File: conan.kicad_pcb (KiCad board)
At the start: 4 copper layers, 313 parts, among them J1 JST-XH, J10 PWM11, J11 PWM3, J12 PWM7, J13 PWM12, J14 PWM4, J15 PWM8, J16 Stepper, J17 Stepper, J18 Stepper, J19 Stepper, J2 JST-XH, J20 Stepper, J21 Stepper, J22 Boot, J23 UART1, J24 UART2, J25 USB_B_Micro, J26 Endstop 1, J27 Endstop 2, J28 Endstop 3, J29 Endstop 4, J3 JTAG, J30 Endstop 5, J31 Endstop 6, J32 Endstop 7, J33 Endstop 8, J34 Watchdog, J35 Thermistor 1, J36 Thermistor 2, J37 Thermistor 3, J38 Thermistor 4, J39 Thermistor 5, J4 PWM9, J40 Thermistor 6, J43 pmod, J44 esp8266, J45 Chain_in, J46 Chain_out, J47 Exp1_L, J48 Display, J49 Exp1_R, J5 PWM5, J50 Vaux in, J51 VM2 in, J52 VM1 in, J53 Vaux in, J54 Exp2_L, J55 Exp2_R, J6 PWM1_HP, J7 PWM10, J8 PWM2_HP, J9 PWM6, Q1 AON7524, Q2 TPH1R405PL, Q3 TPH1R405PL, Q4 AON7524, Q5 AON7524, Q6 AON7524, Q7 AON7524, Q8 AON7524, Q9 Q_NMOS_DGS, SW1 Reset, U1 ECP5U12_CABGA256, U10 TMC2209, U11 TMC2209, U12 TMC2209, U13 TMC2209, U14 AT25xxx, U15 STM32F070CBTx, U16 74VLX244, U17 STWD100, U2 L7986, U3 TLV62569, U4 TLV62569, U5 LP5907MFX-2.5, U6 LP5907MFX-3.3, U7 MIC4127, U8 TMC2209, U9 TMC2209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

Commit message: some escape routing
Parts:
- moved C45 6.85 mm to (145.6, 71.6)
- moved R6 4.87 mm to (145.8, 63.5), turned to 180 degrees
- moved C41 3.22 mm to (142.2, 66.0), turned to 90 degrees
- moved R7 1.67 mm to (143.8, 63.5), turned to 180 degrees
- moved L2 1.64 mm to (145.6, 69.0)
- moved U3 1.26 mm to (144.9, 65.2)
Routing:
- net HOLDN: track 0.00 -> 7.05 mm
- net SPI_SCK: track 0.00 -> 6.25 mm
- net exp2_14: track 0.00 -> 4.90 mm, vias 0 -> 1
- net pmod1_3: track 0.00 -> 4.73 mm, vias 0 -> 1
- net chain_out_out2: track 0.00 -> 4.73 mm, vias 0 -> 1
- net FPGA5: track 0.00 -> 4.73 mm, vias 0 -> 1
- net FPGA4: track 0.00 -> 4.73 mm, vias 0 -> 1
- net ENDSTOP8: track 0.00 -> 4.73 mm, vias 0 -> 1
- net ENDSTOP7: track 0.00 -> 4.73 mm, vias 0 -> 1
- net GND: track 25.7 -> 30.3 mm, vias 5 -> 14
- net SPI_NSS: track 0.00 -> 3.97 mm
- net PWM11: track 0.00 -> 3.93 mm, vias 0 -> 1
- net pmod1_1: track 0.00 -> 3.77 mm, vias 0 -> 1
- net chain_out_in1: track 0.00 -> 3.77 mm, vias 0 -> 1
- net LED3: track 0.00 -> 3.77 mm, vias 0 -> 1
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
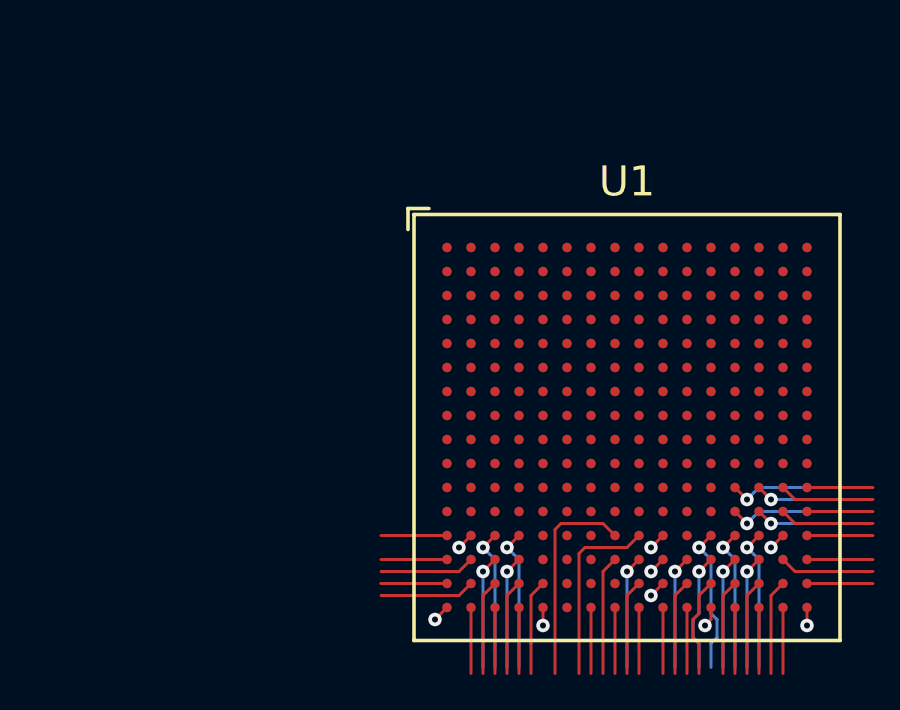
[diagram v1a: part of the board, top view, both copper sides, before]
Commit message: more escape routing
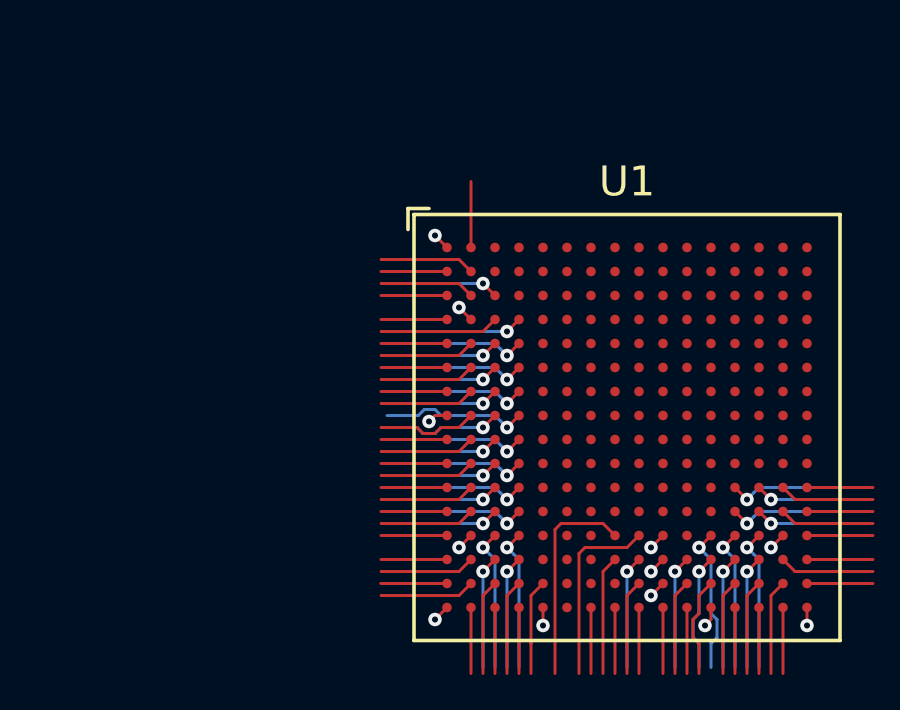
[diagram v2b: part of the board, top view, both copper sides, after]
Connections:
- U1 pad A2: Net-(U1-PadA2) -> exp1_4
- U1 pad A3: Net-(U1-PadA3) -> exp1_3
- U1 pad F5: exp1_3 -> Net-(U1-PadF5)
- U1 pad G5: exp1_4 -> Net-(U1-PadG5)
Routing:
- net exp1_13: track 0.00 -> 4.90 mm, vias 0 -> 1
- net exp1_6: track 0.00 -> 4.73 mm, vias 0 -> 1
- net exp1_12: track 0.00 -> 4.73 mm, vias 0 -> 1
- net exp1_1: track 0.00 -> 4.73 mm, vias 0 -> 1
- net PWM6: track 0.00 -> 4.73 mm, vias 0 -> 1
- net PWM5: track 0.00 -> 4.73 mm, vias 0 -> 1
- net INDEX2: track 0.00 -> 4.73 mm, vias 0 -> 1
- net FPGA2: track 0.00 -> 4.73 mm, vias 0 -> 1
- net INDEX1: track 0.00 -> 4.57 mm, vias 0 -> 1
- net STEP2: track 0.00 -> 3.97 mm
- net exp1_11: track 0.00 -> 3.93 mm, vias 0 -> 1
- net exp1_9: track 0.00 -> 3.77 mm, vias 0 -> 1
- net exp1_17: track 0.00 -> 3.77 mm, vias 0 -> 1
- net exp1_15: track 0.00 -> 3.77 mm, vias 0 -> 1
- net UART2: track 0.00 -> 3.77 mm, vias 0 -> 1
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
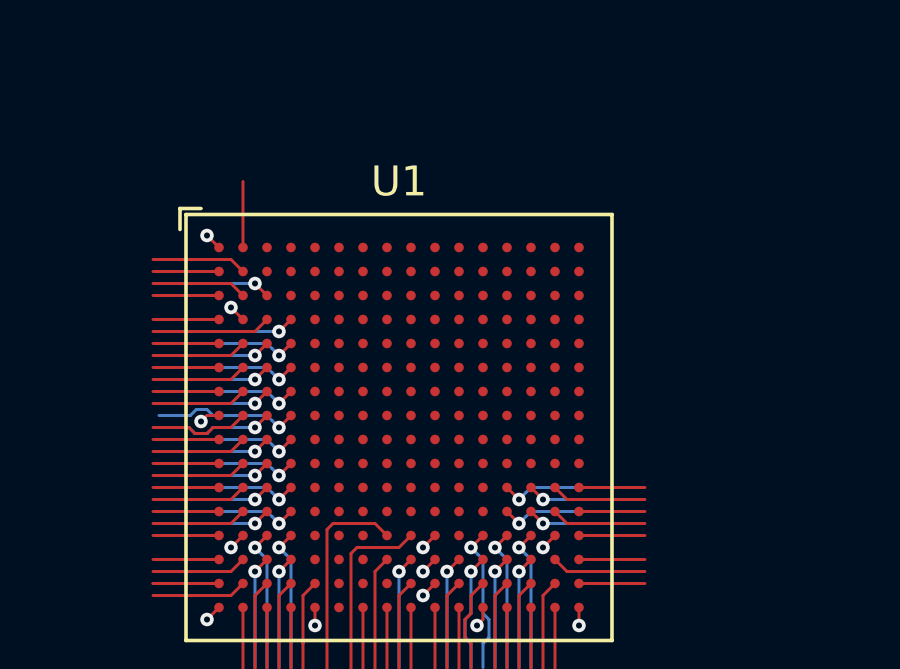
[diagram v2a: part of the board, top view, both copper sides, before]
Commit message: Escape routing done.
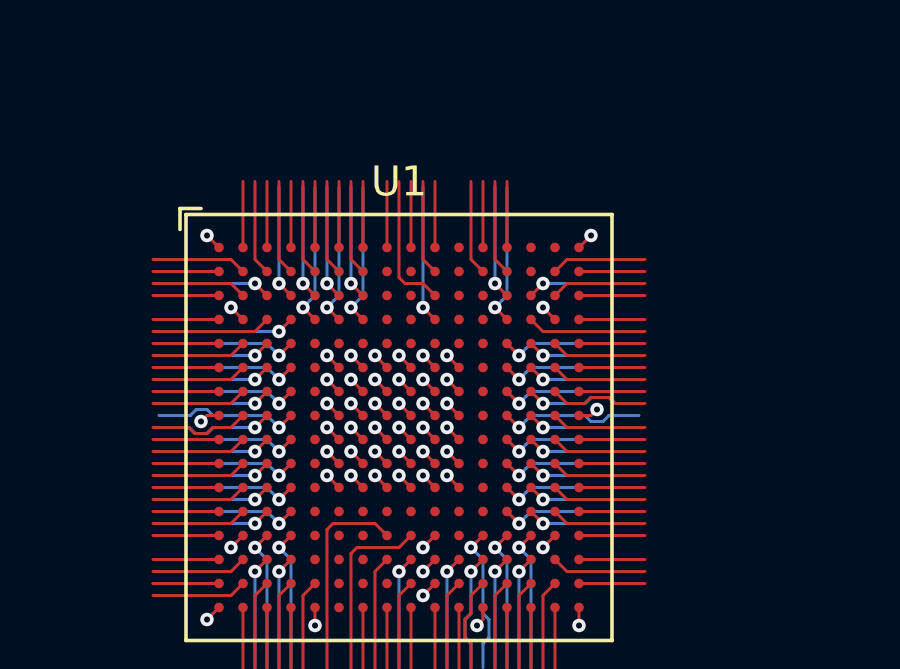
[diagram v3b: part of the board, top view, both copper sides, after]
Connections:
- U1 pad A12: Net-(U1-PadA12) -> ESP_FLASH
- U1 pad B12: Net-(U1-PadB12) -> ESP_GPIO2
- U1 pad C12: ESP_GPIO2 -> Net-(U1-PadC12)
- U1 pad E12: ESP_FLASH -> Net-(U1-PadE12)
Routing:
- net GND: track 32.2 -> 42.4 mm, vias 17 -> 35
- net +3V3: track 2.05 -> 9.40 mm, vias 1 -> 14
- net UART6: track 0.00 -> 4.90 mm, vias 0 -> 1
- net display12: track 0.00 -> 4.73 mm, vias 0 -> 1
- net ESP_RST: track 0.00 -> 4.73 mm, vias 0 -> 1
- net pmod1_4: track 0.00 -> 4.73 mm, vias 0 -> 1
- net exp2_4: track 0.00 -> 4.73 mm, vias 0 -> 1
- net exp2_1: track 0.00 -> 4.73 mm, vias 0 -> 1
- net INDEX4: track 0.00 -> 4.73 mm, vias 0 -> 1
- net ESP_TX: track 0.00 -> 4.73 mm, vias 0 -> 1
- net display8: track 0.00 -> 4.73 mm, vias 0 -> 1
- net display5: track 0.00 -> 4.73 mm, vias 0 -> 1
- net chain_in_out1: track 0.00 -> 4.65 mm
- net chain_in_out2: track 0.00 -> 4.57 mm, vias 0 -> 1
- net exp2_10: track 0.00 -> 3.97 mm
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
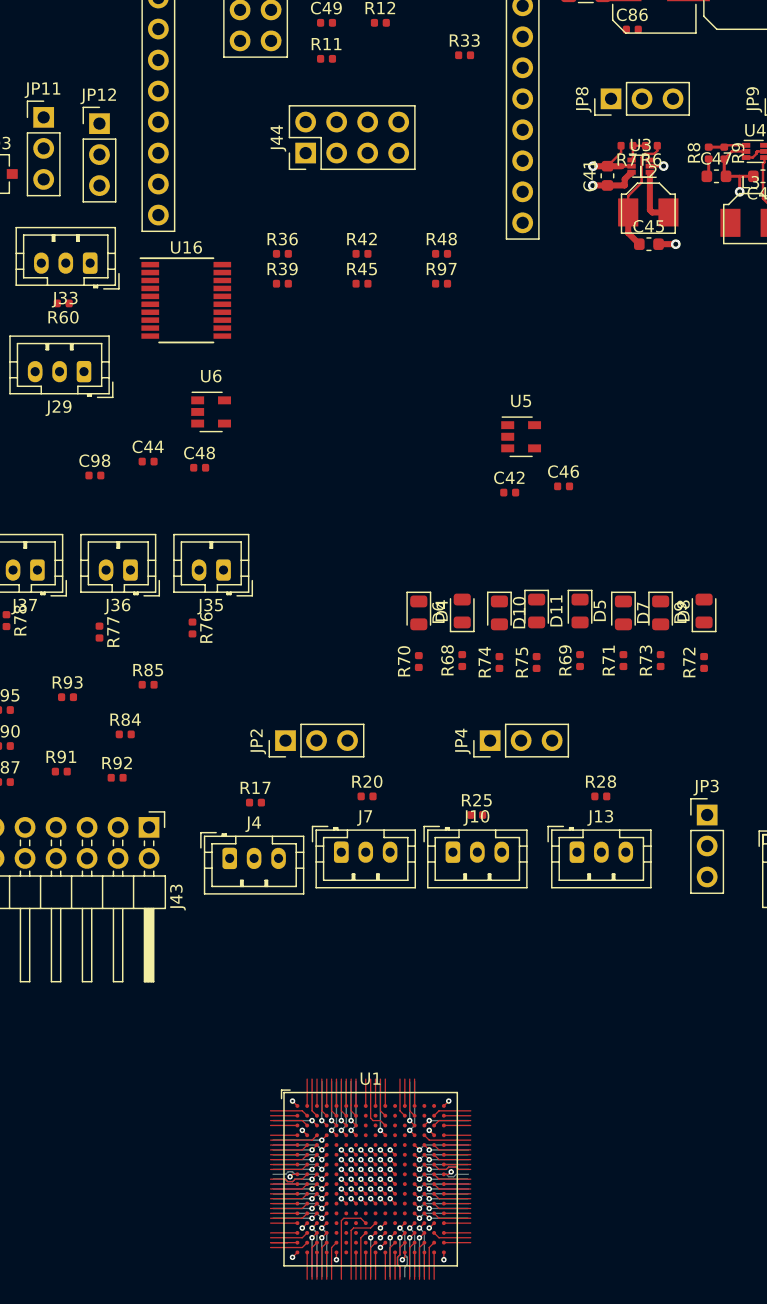
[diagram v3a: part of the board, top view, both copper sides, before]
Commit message: snapshot before going from 0402 to 0603
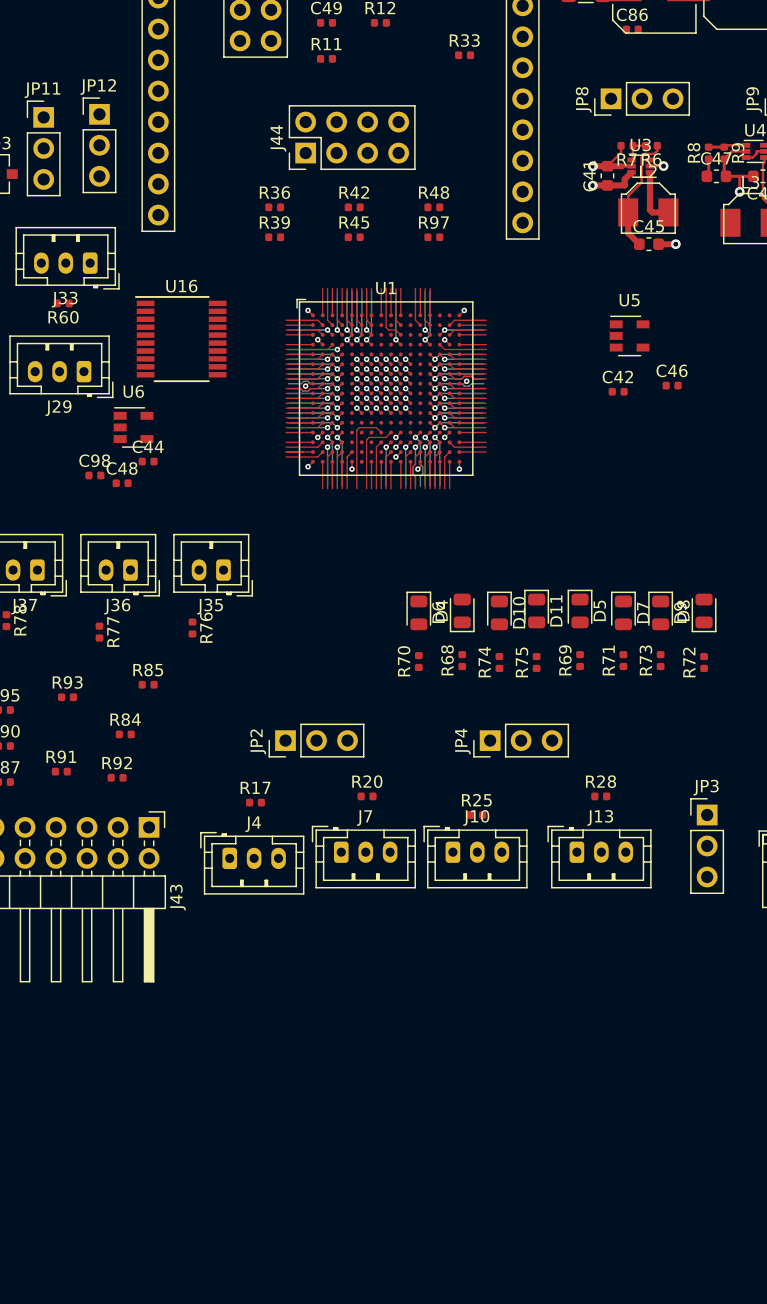
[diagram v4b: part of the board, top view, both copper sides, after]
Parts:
- moved U1 64.8 mm to (124.1, 83.4)
- moved U5 12.1 mm to (144.0, 79.1)
- moved C42 12.1 mm to (143.1, 83.7)
- moved C46 12.1 mm to (147.5, 83.2)
- moved C48 6.48 mm to (102.4, 91.2)
- moved U6 6.48 mm to (103.4, 86.6)
- moved R48 3.86 mm to (128.0, 68.6)
- moved R97 3.86 mm to (128.0, 71.0)
- moved R42 3.86 mm to (121.5, 68.6)
- moved R45 3.86 mm to (121.5, 71.0)
- moved R36 3.86 mm to (114.9, 68.6)
- moved R39 3.86 mm to (114.9, 71.0)
- moved U16 3.20 mm to (107.3, 79.4)
- moved JP12 0.76 mm to (100.6, 61.0)

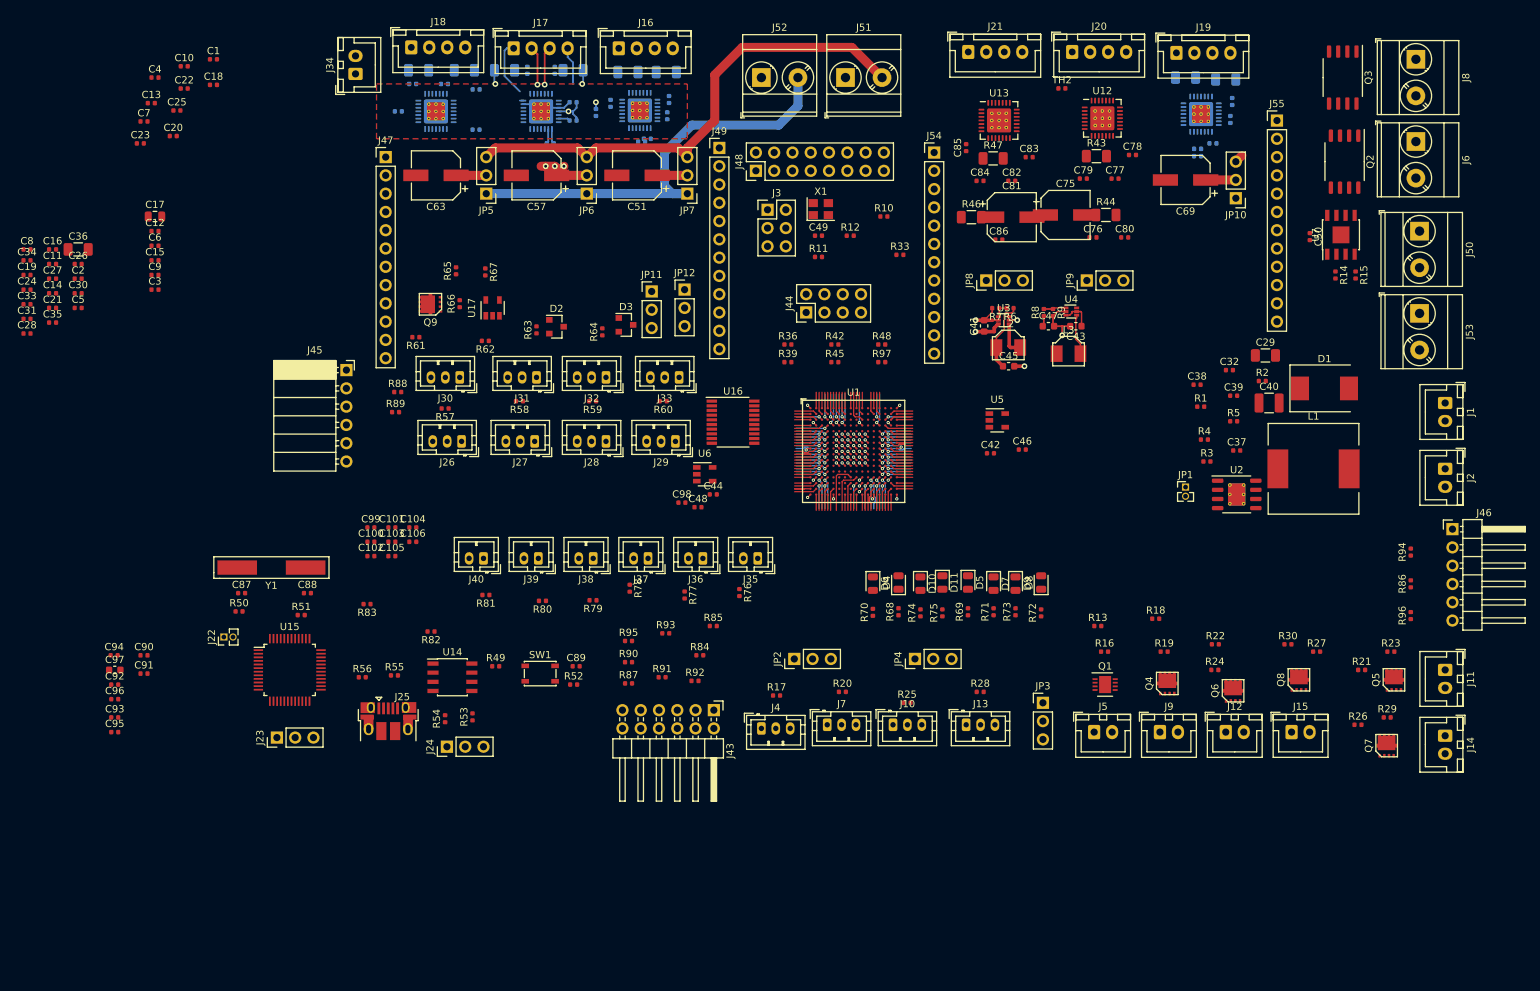
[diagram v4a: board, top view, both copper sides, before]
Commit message: fixed an error in tmc2209 schematic, finished routing one driver
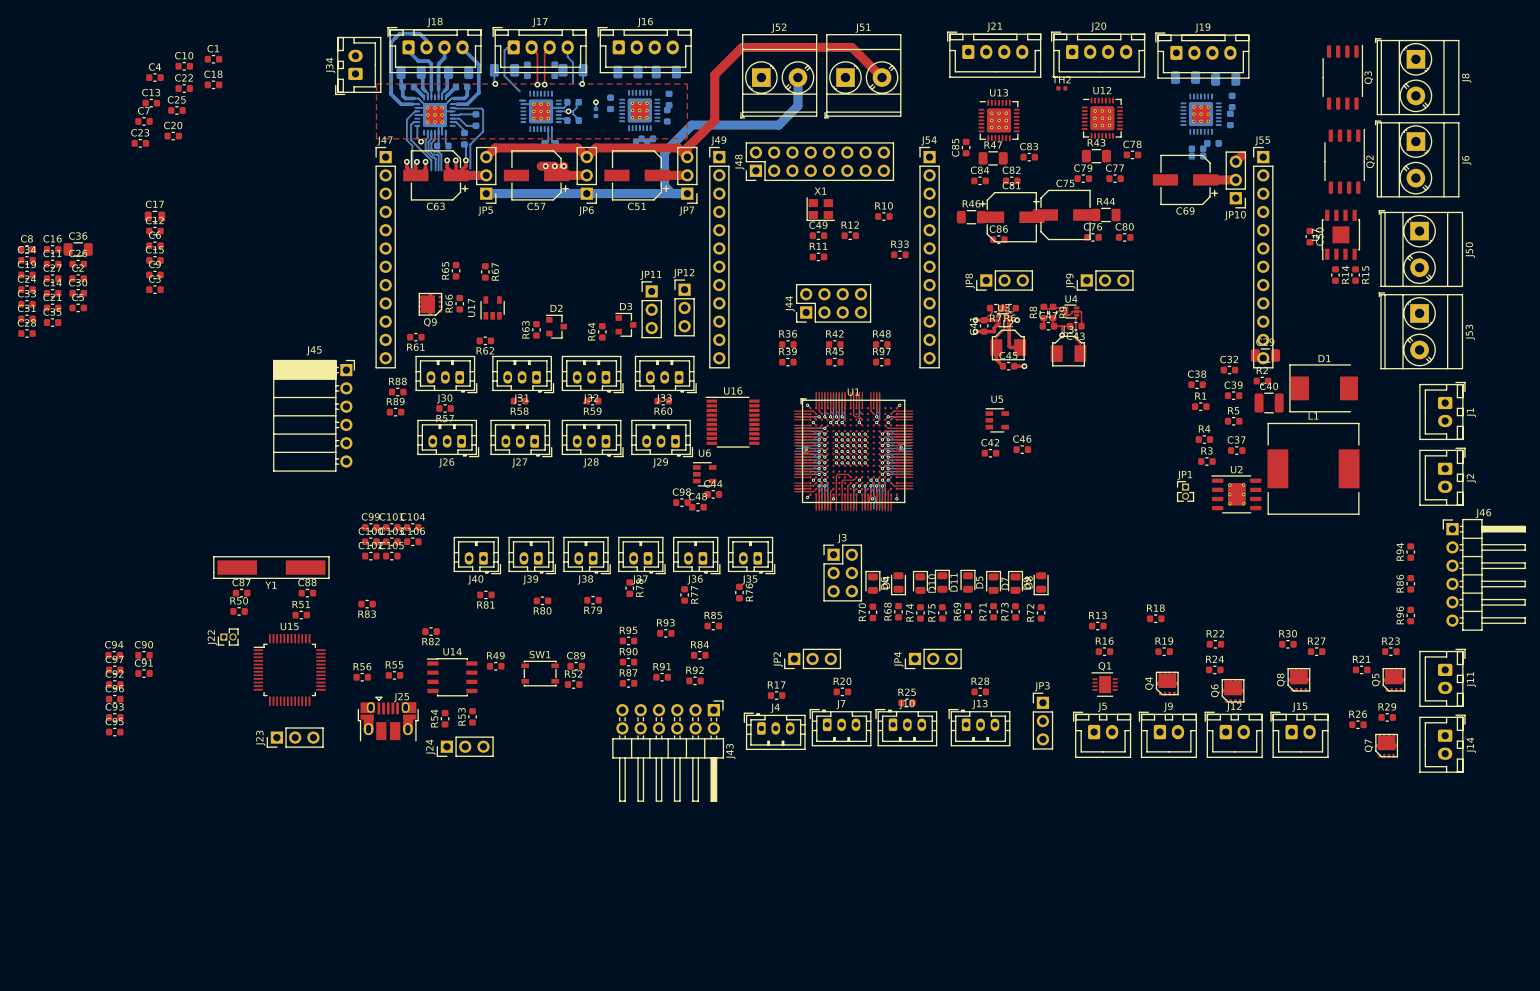
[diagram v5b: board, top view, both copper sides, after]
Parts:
- C1, C10, C100, C101, C102, C103, C104, C105, C106, C11, C12, C13, C14, C15, C16, C18, C19, C2, C20, C21, C22, C23, C24, C25, C26, C27, C28, C3, C30, C31, C32, C33, C34, C35, C37, C38, C39, C4, C42, C44, C46, C48, C49, C5, C50, C52, C53, C54, C55, C56, C58, C59, C6, C60, C61, C62, C64, C65, C66, C67, C68, C7, C70, C71, C72, C73, C74, C76, C77, C78, C79, C8, C80, C82, C83, C84, C85, C86, C87, C88, C89, C9, C90, C91, C92, C93, C94, C95, C96, C98, C99: footprint Capacitor_SMD:C_0402_1005Metric -> Capacitor_SMD:C_0603_1608Metric
- R1, R10, R11, R12, R13, R14, R15, R16, R17, R18, R19, R2, R20, R21, R22, R23, R24, R25, R26, R27, R28, R29, R3, R30, R33, R36, R39, R4, R42, R45, R48, R49, R5, R50, R51, R52, R53, R54, R55, R56, R57, R58, R59, R6, R60, R61, R62, R63, R64, R65, R66, R67, R68, R69, R7, R70, R71, R72, R73, R74, R75, R76, R77, R78, R79, R8, R80, R81, R82, R83, R84, R85, R86, R87, R88, R89, R9, R90, R91, R92, R93, R94, R95, R96, R97: footprint Resistor_SMD:R_0402_1005Metric -> Resistor_SMD:R_0603_1608Metric
- moved J3 48.8 mm to (121.3, 97.8)
- moved C67 9.58 mm to (67.0, 41.0)
- moved C66 8.11 mm to (70.0, 40.0), turned to 270 degrees
- moved J55 5.43 mm to (181.0, 42.5)
- moved C65 3.67 mm to (62.2, 32.8)
- moved C64 2.06 mm to (69.6, 32.8), turned to 0 degrees
- moved C68 1.34 mm to (71.6, 37.4), turned to 270 degrees
- moved J49 1.27 mm to (105.4, 42.5)
- moved R37 1.08 mm to (62.6, 30.8)
- moved J54 0.90 mm to (134.6, 42.5)
- moved R38 0.84 mm to (69.2, 30.8), turned to 0 degrees
- moved U10 0.52 mm to (65.9, 36.7)
- moved J18 0.38 mm to (62.2, 27.3)
- moved J16 0.13 mm to (91.4, 27.3)
- moved J17 0.13 mm to (76.8, 27.3)
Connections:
- C56 pad 1: /Stepper/Stepper 3/VM -> Net-(C56-Pad1)
- C62 pad 1: /Stepper/Stepper 2/VM -> Net-(C62-Pad1)
- C68 pad 1: /Stepper/Stepper 1/VM -> Net-(C68-Pad1)
- C74 pad 1: /Stepper/Stepper 6/VM -> Net-(C74-Pad1)
- C80 pad 1: /Stepper/Stepper 5/VM -> Net-(C80-Pad1)
- C86 pad 1: /Stepper/Stepper 4/VM -> Net-(C86-Pad1)
- U10 pad 4: /Stepper/Stepper 1/VM -> Net-(C68-Pad1)
- U11 pad 4: /Stepper/Stepper 6/VM -> Net-(C74-Pad1)
- U12 pad 4: /Stepper/Stepper 5/VM -> Net-(C80-Pad1)
- U13 pad 4: /Stepper/Stepper 4/VM -> Net-(C86-Pad1)
- U8 pad 4: /Stepper/Stepper 3/VM -> Net-(C56-Pad1)
- U9 pad 4: /Stepper/Stepper 2/VM -> Net-(C62-Pad1)
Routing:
- net GND: track 42.4 -> 76.9 mm, vias 35 -> 38
- net /Stepper/Stepper 1/OA2: track 0.00 -> 20.2 mm
- net /Stepper/Stepper 1/VM: track 4.19 -> 18.3 mm, vias 0 -> 3
- net ENN: track 3.17 -> 16.4 mm
- net /Stepper/Stepper 1/OB2: track 0.00 -> 11.5 mm
- net DIR1: track 2.20 -> 11.5 mm
- net /Stepper/Stepper 1/OA1: track 0.00 -> 9.08 mm
- net STEP1: track 3.17 -> 11.7 mm
- net /Stepper/Stepper 1/OB1: track 0.00 -> 7.28 mm
- net INDEX1: track 4.57 -> 11.0 mm
- net DIAG1: track 3.17 -> 9.56 mm
- net CLK: track 3.17 -> 9.30 mm
- net Net-(R37-Pad1): track 0.00 -> 3.82 mm
- net Net-(R38-Pad1): track 0.00 -> 3.82 mm
- net Net-(C68-Pad2): track 0.00 -> 3.66 mm
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- added copper zone on In2.Cu, net /Stepper/Stepper 1/VM
